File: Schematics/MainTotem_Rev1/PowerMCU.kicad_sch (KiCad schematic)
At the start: 25 parts, among them U1 STM32H757IIT6, U2 ADR4525BRZ-R7

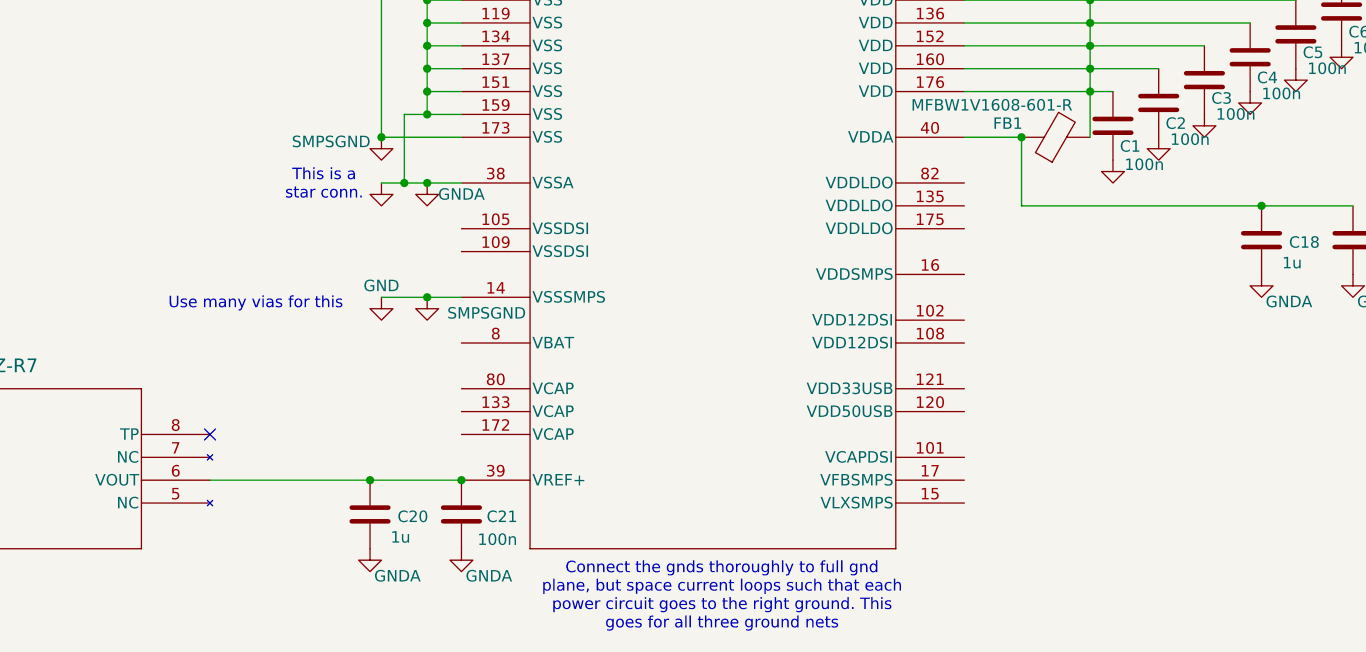
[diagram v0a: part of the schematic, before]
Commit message: Added RS485 functionality to MainTotemLite
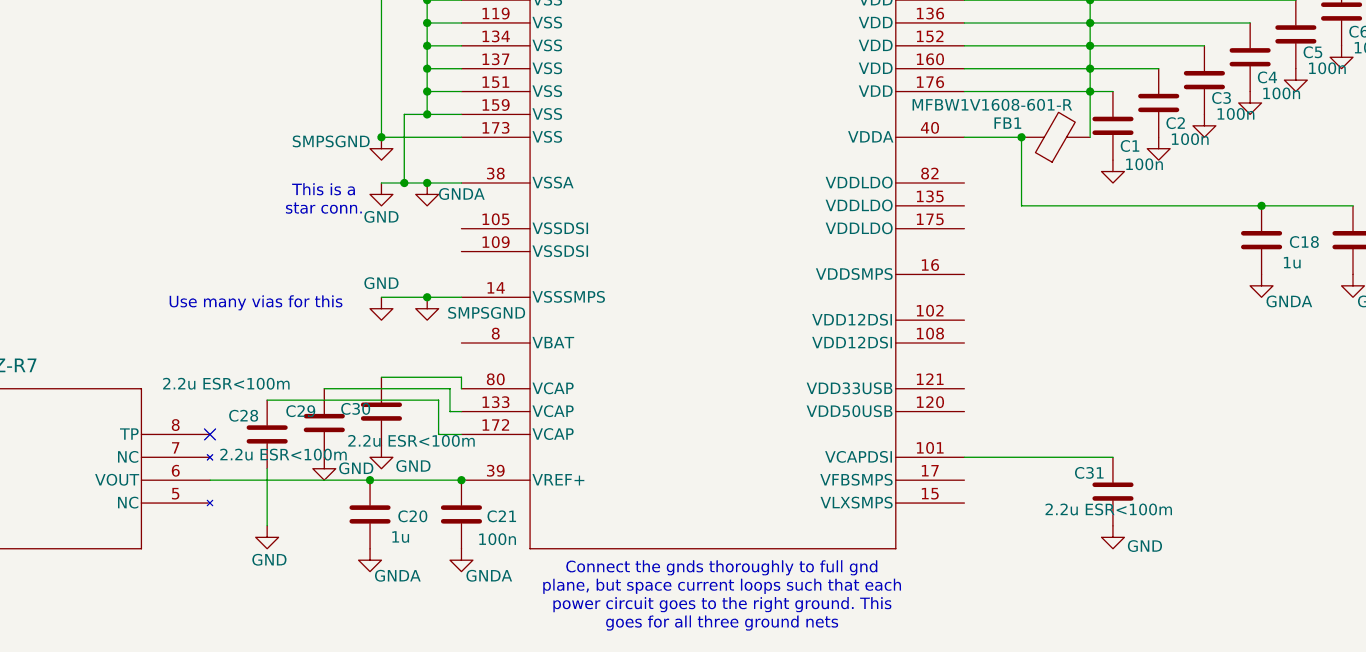
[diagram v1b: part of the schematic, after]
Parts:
- added C28, C29, C30, C31: 2.2u ESR<100m, symbol Device:C
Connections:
- net GND: now also C28.2, C29.2, C30.2, C31.2
- net at U1.101 (VCAPDSI): now also C31.1
- net at U1.133 (VCAP): now also C29.1
- net at U1.172 (VCAP): now also C28.1
- net at U1.80 (VCAP): now also C30.1

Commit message: Adding the MTL Schematics in post editing
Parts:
- added C47, C48, C49, C51, C54: 100n, symbol Device:C
- added C50: 47u, symbol Device:C
- added C55: 4.7u ESR<100m, symbol Device:C
- added C56: 220pF, symbol Device:C
- added C57, C58: 10u ESR<20m, symbol Device:C
- added L1: VLS252012CX-2R2M-1, VLS252012CX-2R2M-1:IND_VLS252012CX-2R2M-1, symbol 22uFInductor:VLS252012CX-2R2M-1
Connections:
- net +3.3V: now also U1.121 (VDD33USB), U1.135 (VDDLDO), U1.16 (VDDSMPS), U1.17 (VFBSMPS), U1.175 (VDDLDO), U1.8 (VBAT), U1.82 (VDDLDO), C47.1, C48.1, C49.1, C50.1, C51.1, C54.1, C55.1, C57.1, C58.1, L1.1
- net GND: now also U1.105 (VSSDSI), U1.109 (VSSDSI), U1.120 (VDD50USB), C47.2, C48.2, C49.2, C50.2, C51.2, C54.2, C55.2, C56.2, C57.2, C58.2
- net at C31.1, U1.101 (VCAPDSI): now also U1.102 (VDD12DSI), U1.108 (VDD12DSI)
- net at U1.15 (VLXSMPS): now also C56.1, L1.2
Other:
- note added: "LDO Supplied by SMPS in order to conserve energy and reduce heat."
- note added: "MIPI DSI supported, USB not supported"
- note added: "Make sure to connect this close to pin 14 so it has an easy path to VSSSMPS"

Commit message: Layout Edits for Mezzanine Connector routing
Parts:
- removed C50: 47u, symbol Device:C
- added C52: 100n, Capacitor_SMD:C_0603_1608Metric_Pad1.08x0.95mm_HandSolder, symbol Device:C
- C1, C10, C11, C12, C13, C14, C15, C16, C17, C18, C19, C2, C20, C21, C22, C28, C29, C3, C30, C31, C4, C47, C48, C49, C5, C51, C54, C55, C56, C6, C7, C8, C9: footprint (none) -> Capacitor_SMD:C_0603_1608Metric_Pad1.08x0.95mm_HandSolder
- C57, C58: footprint (none) -> Capacitor_SMD:C_0805_2012Metric_Pad1.18x1.45mm_HandSolder
- FB1: footprint (none) -> Resistor_SMD:R_0603_1608Metric_Pad0.98x0.95mm_HandSolder
- L1: footprint VLS252012CX-2R2M-1:IND_VLS252012CX-2R2M-1 -> 22uFInductor:IND_VLS252012CX-2R2M-1
- U2: footprint R_8_ADI -> ADR4525BRZ:R_8_ADI-M
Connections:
- net GND: now also C52.2; no longer U1.120 (VDD50USB)
- net at C31.1, U1.101 (VCAPDSI), U1.102 (VDD12DSI)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: now also C52.1
- net +3.3V renamed +3V3
- net +3V3: now also U1.120 (VDD50USB); no longer C47.1, C48.1, C49.1, C57.1, C58.1, L1.1, U1.135 (VDDLDO), U1.17 (VFBSMPS), U1.175 (VDDLDO), U1.82 (VDDLDO)
- new net: C47.1, C48.1, C49.1, C57.1, C58.1, L1.1, U1.135 (VDDLDO), U1.17 (VFBSMPS), U1.175 (VDDLDO), U1.82 (VDDLDO)
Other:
- note added: "MIPI DSI supported, but not connected anywhere, USB not supported but does have a mezzanine connection"
- note removed: "MIPI DSI supported, USB not supported"
